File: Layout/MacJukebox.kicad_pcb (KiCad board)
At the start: 2 copper layers, 39 parts, among them J1 USB_B_Micro, J2 AudioJack2_Ground, J3 Conn_ST_STDC14, U1 LD3985M33R_SOT23, U2 STM32F407VGTx

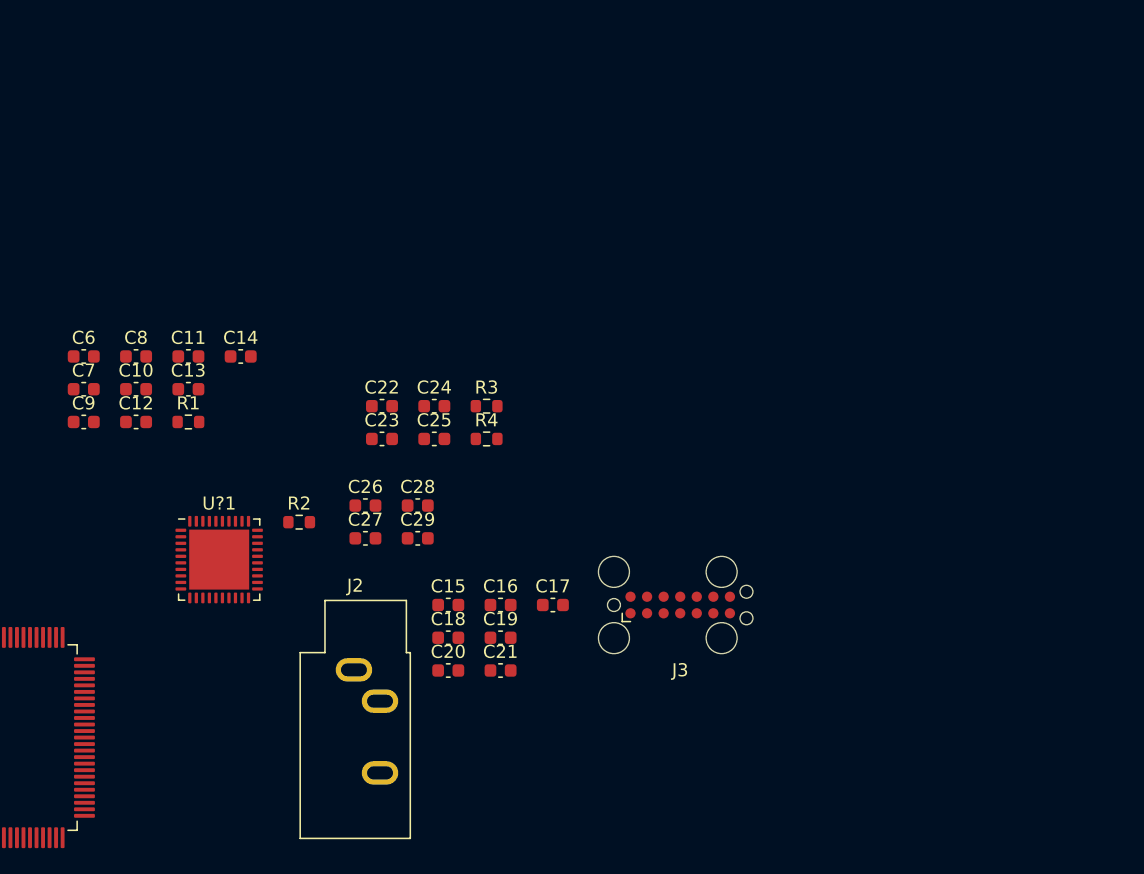
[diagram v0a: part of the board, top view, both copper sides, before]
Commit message: Add USB and LED sections
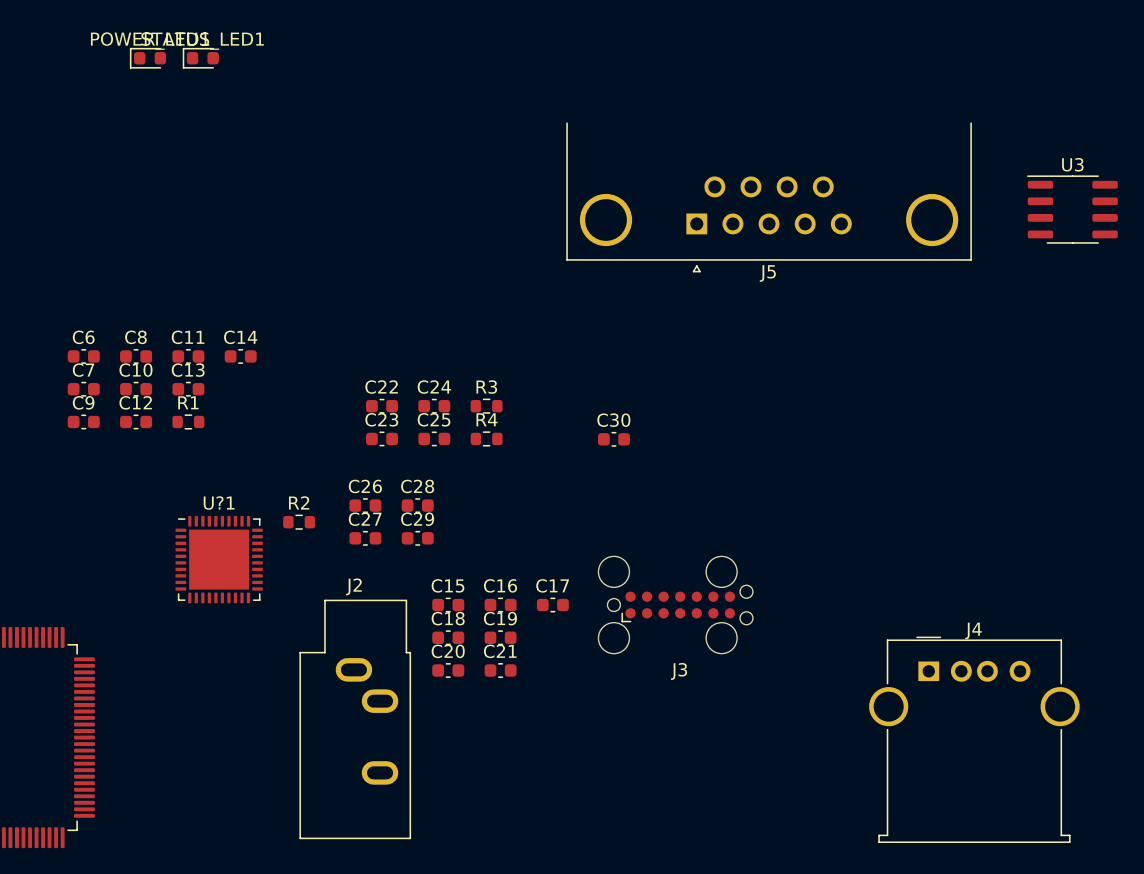
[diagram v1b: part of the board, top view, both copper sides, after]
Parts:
- added C30: 1uF, Capacitor_SMD:C_0603_1608Metric, F.Cu at (181.6, 68.6)
- added J4: USB_A, Connector_USB:USB_A_Molex_67643_Horizontal, F.Cu at (205.7, 86.4)
- added J5: Mac 128/512, Connector_Dsub:DSUB-9_Female_Horizontal_P2.77x2.84mm_EdgePinOffset4.94mm_Housed_MountingHolesOffset7.48mm, F.Cu at (188.0, 52.1)
- added POWER_LED1: RED LED, LED_SMD:LED_0603_1608Metric, F.Cu at (146.1, 39.4)
- added STATUS_LED1: GREEN LED, LED_SMD:LED_0603_1608Metric, F.Cu at (150.1, 39.4)
- added U3: MAX3488, Package_SO:SOIC-8_3.9x4.9mm_P1.27mm, F.Cu at (216.8, 51.0)
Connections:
- net Net-(U2-Pad68) renamed VBUS_SENSE
- C6 pad 1: Net-(C6-Pad1) -> RST
- C6 pad 2: Net-(C6-Pad2) -> GND
- C7 pad 2: Net-(C7-Pad2) -> GND
- C8 pad 2: Net-(C7-Pad2) -> GND
- J3 pad 11: Net-(J3-Pad11) -> GND
- J3 pad 12: Net-(J3-Pad12) -> RST
- J3 pad 13: Net-(J3-Pad13) -> VCP_RX
- J3 pad 14: Net-(J3-Pad14) -> VCP_TX
- J3 pad 3: Net-(J3-Pad3) -> +3V3
- J3 pad 4: Net-(J3-Pad4) -> SWDIO
- J3 pad 5: Net-(J3-Pad5) -> GND
- J3 pad 6: Net-(J3-Pad6) -> SWCLK
- J3 pad 7: Net-(J3-Pad5) -> GND
- J3 pad 8: Net-(J3-Pad8) -> SWO
- R1 pad 2: Net-(C6-Pad1) -> RST
- U2 pad 14: Net-(C6-Pad1) -> RST
- U2 pad 23: Net-(U2-Pad23) -> VCP_RX
- U2 pad 24: Net-(U2-Pad24) -> VCP_TX
- U2 pad 36: Net-(U2-Pad36) -> STATUS_LED
- U2 pad 70: Net-(U2-Pad70) -> USB_D-
- U2 pad 71: Net-(U2-Pad71) -> USB_D+
- U2 pad 72: Net-(U2-Pad72) -> SWDIO
- U2 pad 76: Net-(U2-Pad76) -> SWCLK
- U2 pad 89: Net-(U2-Pad89) -> SWO
- U2 pad 94: Net-(C6-Pad2) -> GND

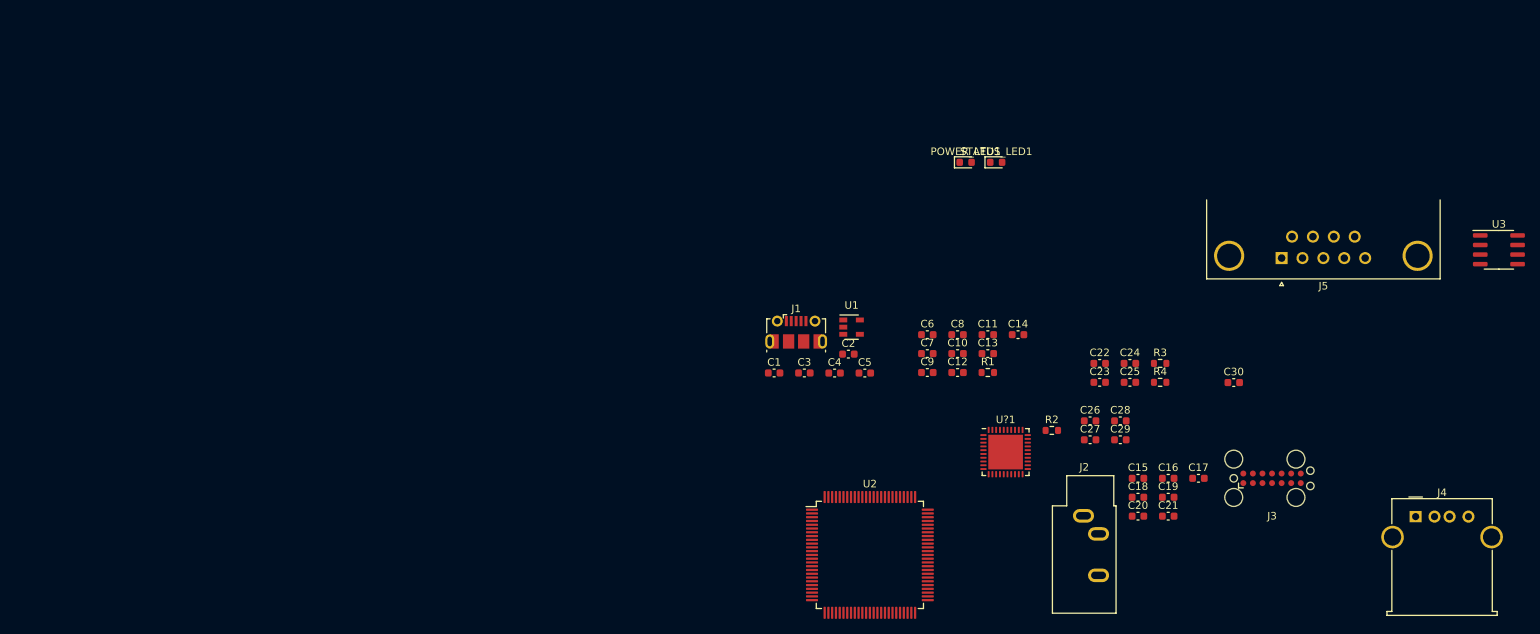
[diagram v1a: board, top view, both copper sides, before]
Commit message: Enable USB device, start laying out board
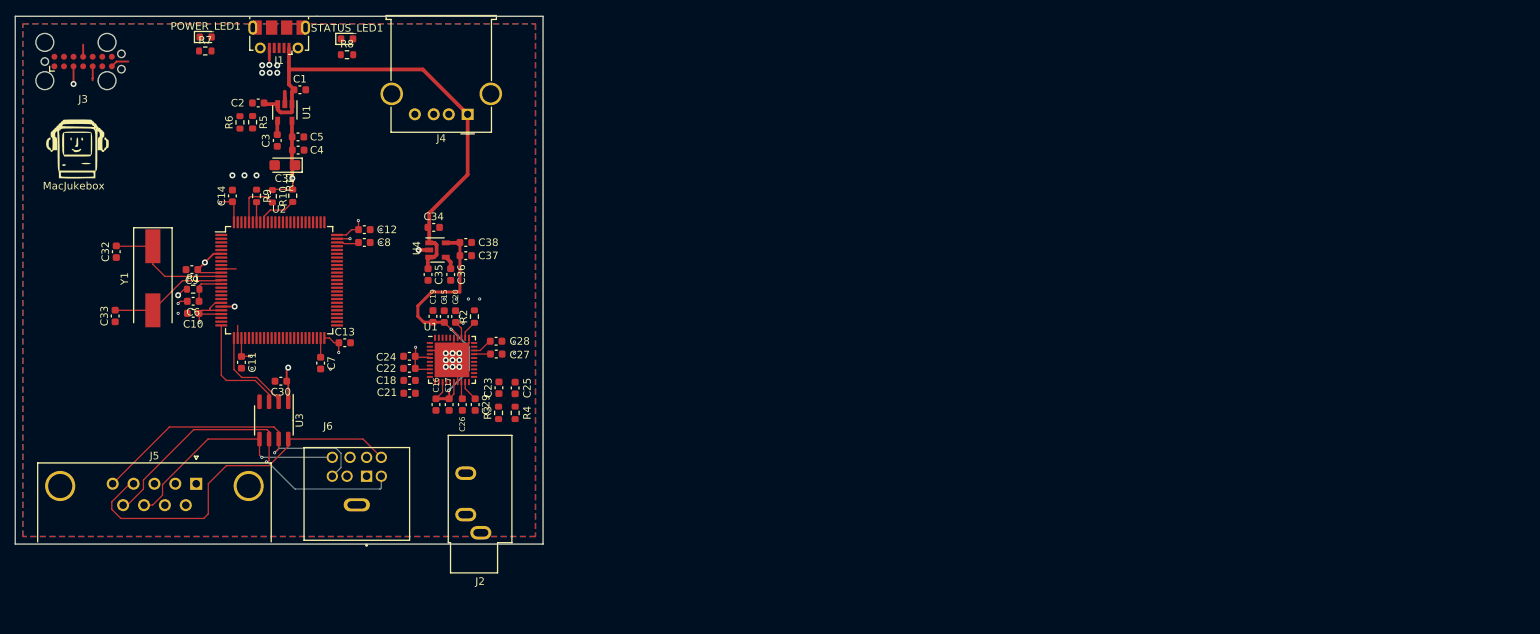
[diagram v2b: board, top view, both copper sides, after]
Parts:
- added C31: 10uF, Capacitor_Tantalum_SMD:CP_EIA-3216-18_Kemet-A, F.Cu at (55.8, 39.8)
- added C32: 18pF, Capacitor_SMD:C_0603_1608Metric, F.Cu at (33.4, 51.2)
- added C33: 18pF, Capacitor_SMD:C_0603_1608Metric, F.Cu at (33.2, 59.8)
- added C34: 1uF, Capacitor_SMD:C_0603_1608Metric, F.Cu at (75.5, 48.0)
- added C35: 100nF, Capacitor_SMD:C_0603_1608Metric, F.Cu at (74.8, 54.2)
- added C36: 10nF, Capacitor_SMD:C_0603_1608Metric, F.Cu at (77.8, 54.2)
- added C37: 1uF, Capacitor_SMD:C_0603_1608Metric, F.Cu at (79.8, 51.8)
- added C38: 100nF, Capacitor_SMD:C_0603_1608Metric, F.Cu at (79.8, 50.0)
- added G***: LOGO, MacJukebox:logo, F.Cu at (28.2, 37.5)
- added J6: Mini-DIN-8, MacJukebox:CUI_MD-80S, F.Cu at (65.3, 83.3)
- added R10: 4.7K, Resistor_SMD:R_0603_1608Metric, F.Cu at (54.1, 43.9)
- added R11: 4.7K, Resistor_SMD:R_0603_1608Metric, F.Cu at (56.8, 43.8)
- added R5: 1K, Resistor_SMD:R_0603_1608Metric, F.Cu at (51.5, 34.0)
- added R6: 2.4K, Resistor_SMD:R_0603_1608Metric, F.Cu at (49.8, 34.1)
- added R7: 200, Resistor_SMD:R_0603_1608Metric, F.Cu at (45.2, 24.6)
- added R8: 200, Resistor_SMD:R_0603_1608Metric, F.Cu at (64.0, 25.1)
- added R9: 10K, Resistor_SMD:R_0603_1608Metric, F.Cu at (52.0, 43.8)
- added U4: LD3985M25R_SOT23, Package_TO_SOT_SMD:SOT-23-5, F.Cu at (76.0, 51.0)
- added Y1: Crystal, Crystal:Crystal_SMD_HC49-SD, F.Cu at (38.2, 54.8)
- moved J3 167.1 mm to (29.0, 26.0)
- moved U3 164.0 mm to (54.3, 73.6), turned to 270 degrees
- moved J5 147.0 mm to (44.0, 82.0), turned to 0 degrees
- moved J4 136.6 mm to (80.0, 33.0), turned to 180 degrees
- moved C30 126.4 mm to (55.2, 68.4), turned to 180 degrees
- moved R1 106.0 mm to (43.6, 56.2)
- moved C14 105.8 mm to (48.8, 43.8), turned to 90 degrees
- moved POWER_LED1 102.2 mm to (45.2, 22.8)
- moved C21 101.9 mm to (72.3, 70.0)
- moved C10 101.5 mm to (43.6, 59.4), turned to 180 degrees
- moved C19 100.4 mm to (75.4, 59.8), turned to 90 degrees
- moved C17 99.9 mm to (77.5, 71.5), turned to 270 degrees
- moved C11 99.1 mm to (50.0, 65.9), turned to 270 degrees
- moved C9 98.5 mm to (43.4, 53.6), turned to 180 degrees
- moved C18 97.8 mm to (72.3, 68.3)
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- renumbered U?1 to U1
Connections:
- net USB_D+ renamed USB_STORAGE_D+
- net USB_D- renamed USB_STORAGE_D-
- J1 pad 2: Net-(J1-Pad2) -> USB_COMPUTER_D-
- J1 pad 3: Net-(J1-Pad3) -> USB_COMPUTER_D+
- J5 pad 4: Net-(J5-Pad4) -> RS422_RX+
- J5 pad 5: Net-(J5-Pad5) -> RS422_RX-
- J5 pad 8: Net-(J5-Pad8) -> RS422_TX+
- J5 pad 9: Net-(J5-Pad9) -> RS422_TX-
- U2 pad 12: Net-(U2-Pad12) -> PH0
- U2 pad 13: Net-(U2-Pad13) -> PH1
- U2 pad 21: Net-(U2-Pad21) -> +3V3
- U2 pad 25: Net-(U2-Pad25) -> DI
- U2 pad 26: Net-(U2-Pad26) -> RO
- U2 pad 52: Net-(U2-Pad52) -> VBUS_SENSE
- U2 pad 53: Net-(U2-Pad53) -> USB_COMPUTER_D-
- U2 pad 54: Net-(U2-Pad54) -> USB_COMPUTER_D+
- U2 pad 94: GND -> Net-(R9-Pad2)
- U3 pad 5: Net-(U3-Pad5) -> RS422_TX+
- U3 pad 6: Net-(U3-Pad6) -> RS422_TX-
- U3 pad 7: Net-(U3-Pad7) -> RS422_RX-
- U3 pad 8: Net-(U3-Pad8) -> RS422_RX+
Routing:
- net +5V: track 0.00 -> 64.0 mm
- net +3V3: track 0.00 -> 63.9 mm, vias 0 -> 12
- net RS422_RX+: track 0.00 -> 49.4 mm
- net RS422_TX-: track 0.00 -> 46.9 mm, vias 0 -> 1
- net RS422_RX-: track 0.00 -> 41.9 mm, vias 0 -> 1
- net +2V5: track 0.00 -> 41.0 mm, vias 0 -> 2
- net GND: track 0.00 -> 33.3 mm, vias 0 -> 33
- net RS422_TX+: track 0.00 -> 31.7 mm, vias 0 -> 1
- net PH0: track 0.00 -> 17.0 mm
- net PH1: track 0.00 -> 15.7 mm
- net DI: track 0.00 -> 15.0 mm
- net RO: track 0.00 -> 12.1 mm
- net PB9: track 0.00 -> 6.71 mm
- net PB6: track 0.00 -> 5.39 mm
- net RST: track 0.00 -> 5.31 mm
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- added copper zone on In1.Cu, net +3V3
- added copper zone on B.Cu, net GND
- added copper zone on F.Cu, net GND
- added copper zone on In2.Cu, net GND
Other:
- board outline added: 70 x 70 mm
- copper layers 2 -> 4
- rule trace_min: 0.2 -> 0.127
- rule via_min_drill: 0.3 -> 0.2
- rule via_min_size: 0.4 -> 0.2
- board text added: "MacJukebox"

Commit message: Finish first layout of board
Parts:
- added G***: LOGO, MacJukebox:ravenswurk, F.Cu at (40.5, 69.6)
- J2: value AudioJack2_Ground -> AudioJack3
- moved STATUS_LED1 64.2 mm to (74.7, 86.3), turned to 90 degrees
- moved R8 54.4 mm to (74.7, 78.4), turned to 270 degrees
- moved G*** 29.5 mm to (26.8, 67.0)
- moved C35 0.33 mm to (74.8, 54.6)
- moved C36 0.33 mm to (77.8, 54.6)
- moved J2 0.16 mm to (81.7, 88.3)
- moved R6 0.10 mm to (49.7, 34.0)
- turned C18 to 180 degrees
- turned C21 to 180 degrees
- renumbered U1 to U?1
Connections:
- J2 pad R: (no net) -> Net-(C25-Pad2)
- J2 pad S: Net-(C25-Pad2) -> GND
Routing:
- net VCP_TX: track 0.00 -> 61.9 mm, vias 0 -> 2
- net VCP_RX: track 0.00 -> 60.1 mm, vias 0 -> 2
- net USB_COMPUTER_D+: track 0.00 -> 58.6 mm, vias 0 -> 2
- net USB_COMPUTER_D-: track 0.00 -> 58.6 mm, vias 0 -> 2
- net RST: track 5.31 -> 61.4 mm, vias 0 -> 2
- net SWDIO: track 0.00 -> 53.3 mm, vias 0 -> 2
- net SWCLK: track 0.00 -> 49.8 mm, vias 0 -> 2
- net VBUS_SENSE: track 0.00 -> 49.0 mm, vias 0 -> 2
- net SWO: track 0.00 -> 45.1 mm, vias 0 -> 2
- net PD4: track 2.81 -> 43.3 mm, vias 0 -> 2
- net PB9: track 6.71 -> 43.6 mm, vias 0 -> 2
- net PB6: track 5.39 -> 39.3 mm, vias 0 -> 2
- net Net-(C25-Pad2): track 0.00 -> 33.0 mm, vias 0 -> 2
- net STATUS_LED: track 0.00 -> 32.1 mm
- net Net-(C23-Pad2): track 0.00 -> 30.8 mm, vias 0 -> 2
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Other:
- board text added: "1.0"
- board text added: "Mac Jukebox"

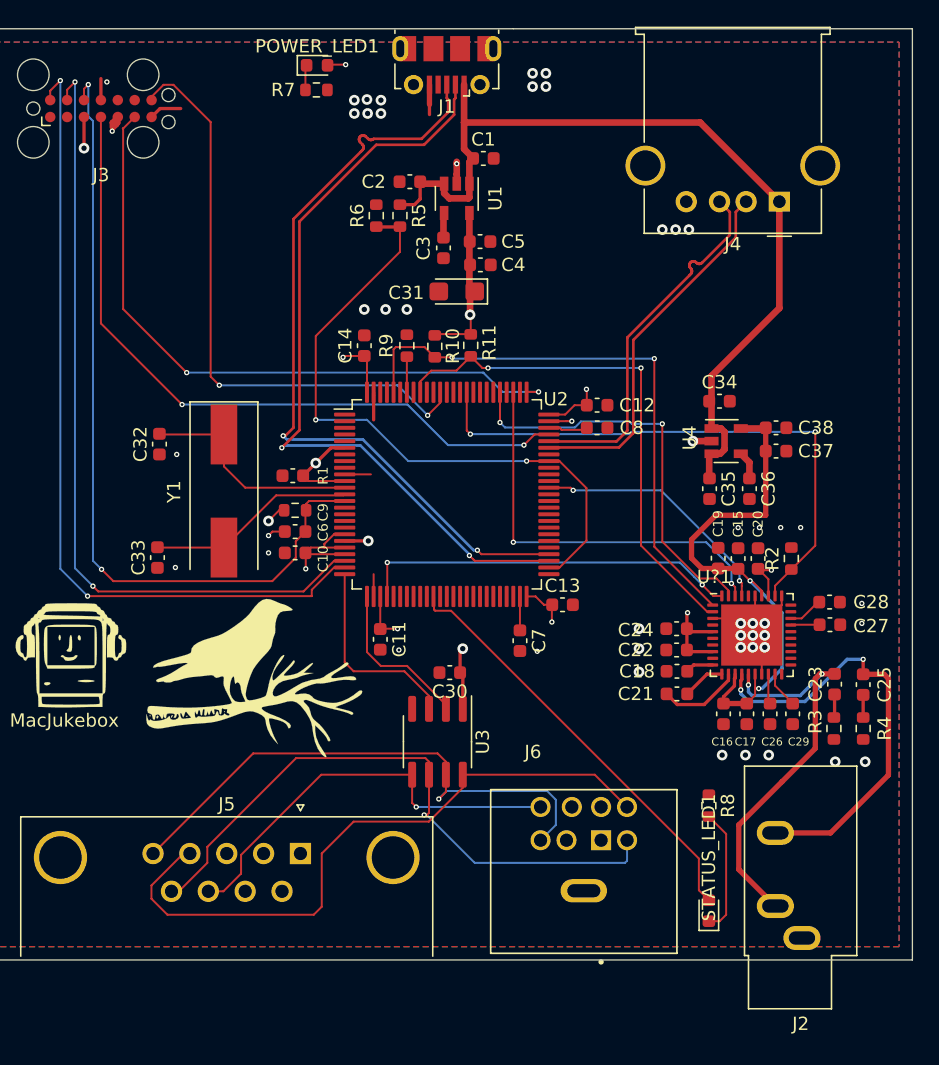
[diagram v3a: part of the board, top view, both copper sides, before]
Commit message: Final corrections, submitted board to fab house
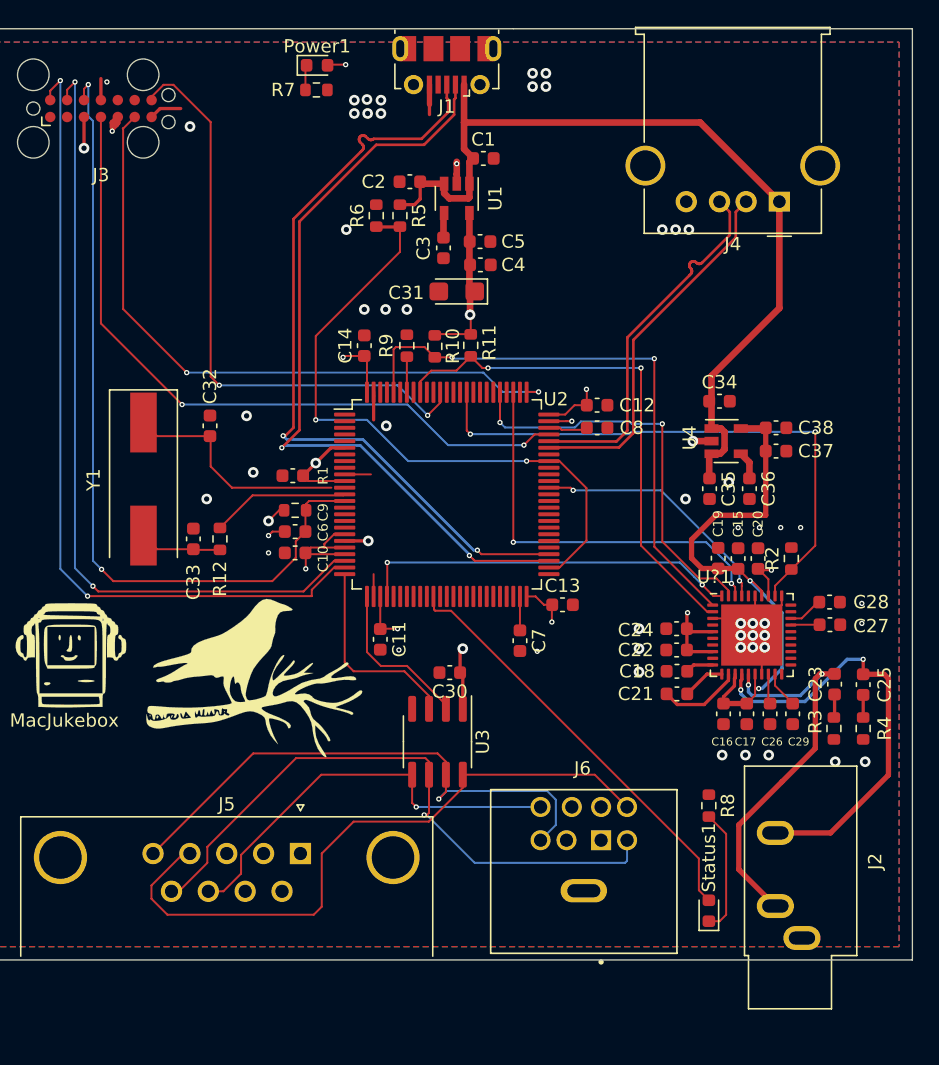
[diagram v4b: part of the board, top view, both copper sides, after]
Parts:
- added R12: 1.1K, Resistor_SMD:R_0603_1608Metric, F.Cu at (38.0, 58.4)
- moved Y1 6.12 mm to (32.2, 53.9)
- moved C32 4.04 mm to (37.2, 49.9), turned to 270 degrees
- moved C33 3.04 mm to (36.0, 58.4), turned to 270 degrees
- renumbered POWER_LED1 to Power1, STATUS_LED1 to Status1
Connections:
- C33 pad 2: PH1 -> Net-(C33-Pad2)
- Y1 pad 2: PH1 -> Net-(C33-Pad2)
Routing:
- net Net-(C33-Pad2): track 0.00 -> 6.20 mm
- net PH1: track 15.7 -> 10.4 mm
- net PH0: track 17.0 -> 17.6 mm
- net GND: vias 51 -> 57
